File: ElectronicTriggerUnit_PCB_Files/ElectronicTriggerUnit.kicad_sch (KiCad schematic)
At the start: 50 parts, among them IC1 MCP1407-E_SN, IC2 ATTINY814-SSF, IC3 BU4S584G2-TR, J2 Conn_01x05, J4 Conn_01x04, M1 Motor_DC, Q1 LC191PTDT, Q2 LKPT30102B-A01, Q3 SIR500DP-T1-RE3, Q4 LC191PTDT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

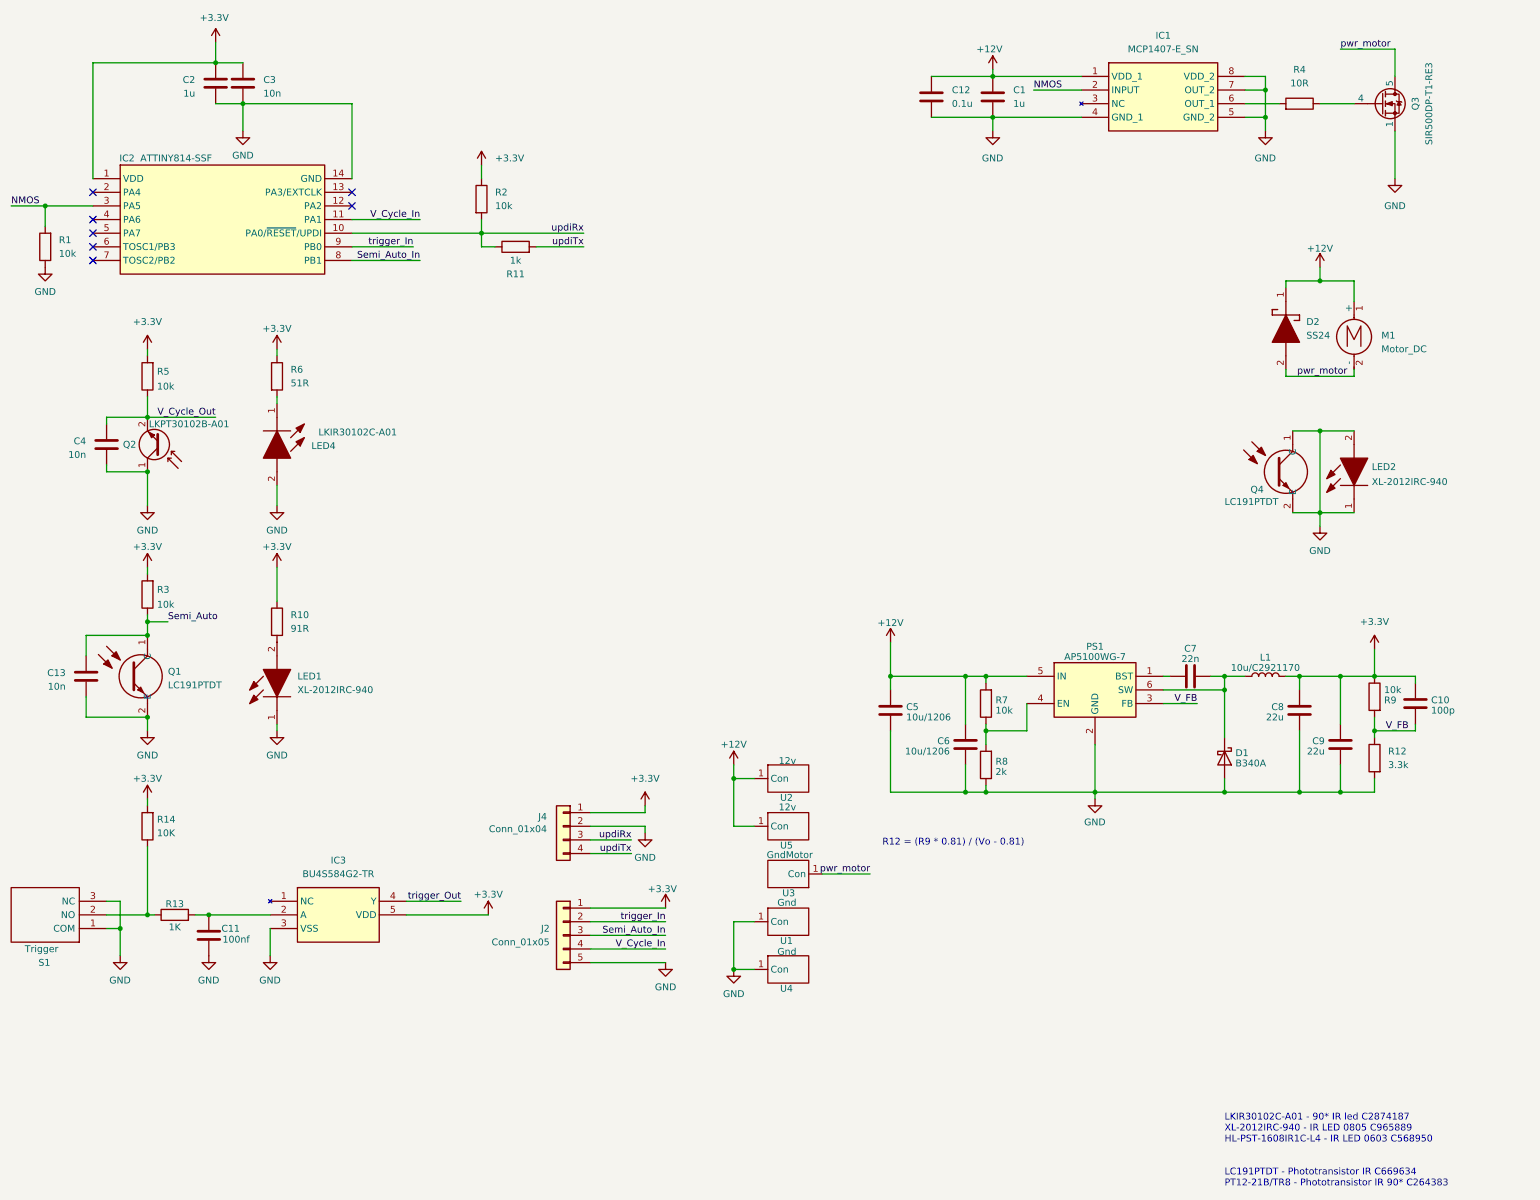
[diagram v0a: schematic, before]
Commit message: added motor ring
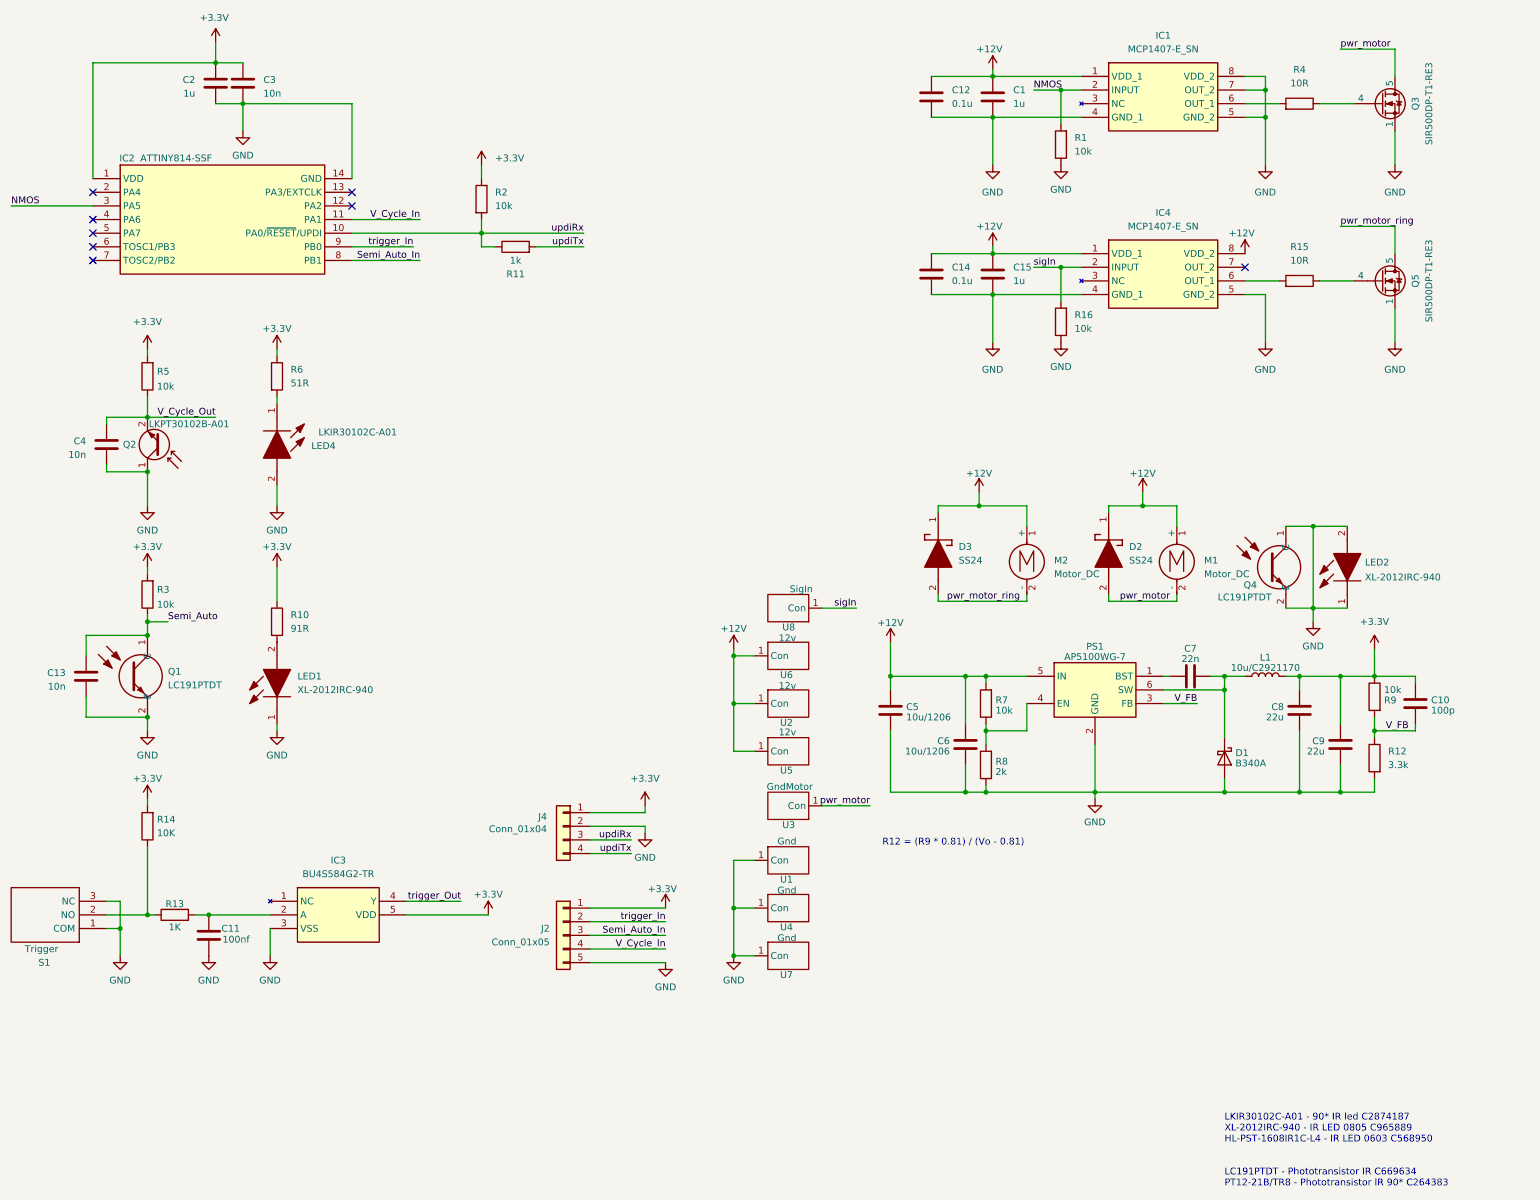
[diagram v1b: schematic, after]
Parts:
- added C14: 0.1u, Capacitor_SMD:C_0603_1608Metric, symbol Device:C
- added C15: 1u, Capacitor_SMD:C_0603_1608Metric, symbol Device:C
- added D3: SS24, SamacSys:DIOM5436X247N, symbol SamacSys:SS24
- added IC4: MCP1407-E_SN, SamacSys:SOIC127P600X175-8N, symbol SamacSys:MCP1407-E_SN
- added M2: Motor_DC, symbol Motor:Motor_DC
- added Q5: SIR500DP-T1-RE3, SamacSys:POWERPAKSO-8, symbol Simulation_SPICE:NMOS
- added R15: 10R, Resistor_SMD:R_1206_3216Metric, symbol Device:R
- added R16: 10k, Resistor_SMD:R_0603_1608Metric, symbol Device:R
- added U6: 12v, SamacSys:Copper_Pad, symbol Copper_Pad:Copper_pad
- added U7: Gnd, SamacSys:Copper_Pad, symbol Copper_Pad:Copper_pad
- added U8: SigIn, SamacSys:Copper_Pad, symbol Copper_Pad:Copper_pad
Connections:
- net +12V: now also C14.1, C15.2, D3.1 (K), IC4.1 (VDD_1), IC4.8 (VDD_2), M2.1 (+), U6.1 (Con)
- net GND: now also C14.2, C15.1, IC4.4 (GND_1), IC4.5 (GND_2), Q5.1, Q5.2, Q5.3, R16.1, U7.1 (Con)
- new net: IC4.6 (OUT_1), R15.2
- new net: Q5.4, R15.1
- new net pwr_motor_ring: D3.2 (A), M2.2 (-), Q5.5, Q5.6, Q5.7, Q5.8, Q5.9
- new net sigIn: IC4.2 (INPUT), R16.2, U8.1 (Con)
- no-connect marks 7 -> 8
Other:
- moved on the sheet: D2, LED2, M1, Q4, R1, U1, U2, U3, U4, U5

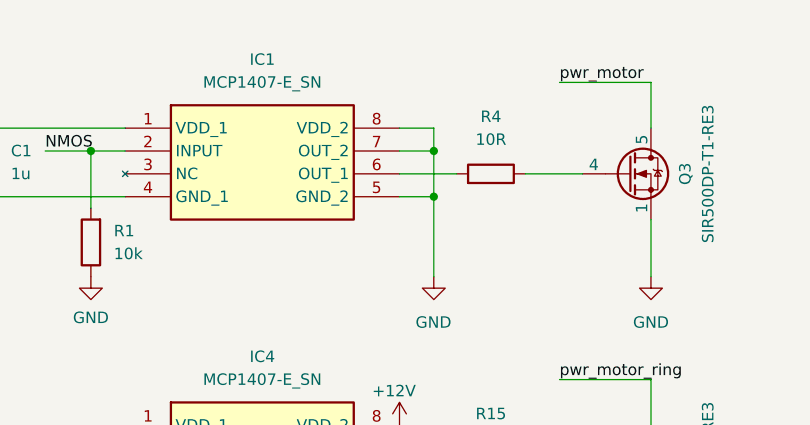
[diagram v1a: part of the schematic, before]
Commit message: outputs of gate driver needed to be shorted :(
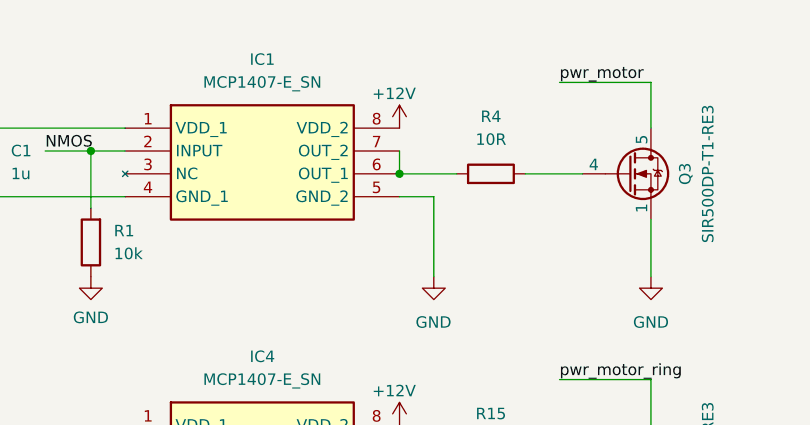
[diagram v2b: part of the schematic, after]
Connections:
- net +12V: now also IC1.8 (VDD_2)
- net GND: no longer IC1.7 (OUT_2), IC1.8 (VDD_2)
- net at IC1.6 (OUT_1), R4.2: now also IC1.7 (OUT_2)
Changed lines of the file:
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@@
 	)
 	(junction
-		(at 248.92 27.94)
-		(diameter 0)
-		(color 0 0 0 0)
-	)
-	(junction
 		(at 226.06 105.41)
 		(diameter 0)
@@
 	)
 	(junction
+		(at 245.11 30.48)
+		(diameter 0)
+		(color 0 0 0 0)
+	)
+	(junction
 		(at 198.12 66.04)
 		(diameter 0)
@@
 	)
 	(junction
-		(at 248.92 33.02)
-		(diameter 0)
-		(color 0 0 0 0)
-	)
-	(junction
 		(at 196.85 137.16)
 		(diameter 0)
@@
 	(wire
 		(pts
-			(xy 248.92 27.94) (xy 248.92 33.02)
-		)
-		(stroke
-			(width 0)
-			(type default)
-		)
-	)
-	(wire
-		(pts
 			(xy 149.86 133.35) (xy 149.86 142.24)
 		)
@@
 	(wire
 		(pts
-			(xy 245.11 27.94) (xy 248.92 27.94)
-		)
-		(stroke
-			(width 0)
-			(type default)
-		)
-	)
-	(wire
-		(pts
 			(xy 269.24 132.08) (xy 269.24 137.16)
 		)
@@
 	(wire
 		(pts
-			(xy 245.11 25.4) (xy 248.92 25.4)
-		)
-		(stroke
-			(width 0)
-			(type default)
-		)
-	)
-	(wire
-		(pts
 			(xy 186.69 58.42) (xy 198.12 58.42)
 		)
@@
 	(wire
 		(pts
+			(xy 245.11 27.94) (xy 245.11 30.48)
+		)
+		(stroke
+			(width 0)
+			(type default)
+		)
+	)
+	(wire
+		(pts
 			(xy 276.86 137.16) (xy 276.86 138.43)
 		)
@@
 	(wire
 		(pts
-			(xy 248.92 25.4) (xy 248.92 27.94)
-		)
-		(stroke
-			(width 0)
-			(type default)
-		)
-	)
-	(wire
-		(pts
 			(xy 40.64 76.2) (xy 40.64 77.47)
 		)
@@
 					(unit 1)
 				)
+			)
+		)
+	)
+	(symbol
+		(lib_name "+12V_1")
+		(lib_id "power:+12V")
+		(at 245.11 25.4 0)
+		(unit 1)
+		(exclude_from_sim no)
+		(in_bom yes)
+		(on_board yes)
+		(dnp no)
+		(property "Reference" "#PWR040"
+			(at 245.11 29.21 0)
+			(effects
+				(font
+					(size 1.27 1.27)
+				)
+				(hide yes)
+			)
+		)
+		(property "Value" "+12V"
+			(at 242.062 21.59 0)
+			(effects
+				(font
+					(size 1.27 1.27)
+				)
+				(justify left)
+			)
+		)
+		(property "Footprint" ""
+			(at 245.11 25.4 0)
+			(effects
+				(font
+					(size 1.27 1.27)
+				)
+				(hide yes)
+			)
+		)
+		(property "Datasheet" ""
+			(at 245.11 25.4 0)
+			(effects
+				(font
+					(size 1.27 1.27)
+				)
+				(hide yes)
+			)
+		)
+		(property "Description" "Power symbol creates a global label with name \"+12V\""
+			(at 245.11 25.4 0)
+			(effects
+				(font
+					(size 1.27 1.27)
+				)
+				(hide yes)
+			)
+		)
+		(pin "1"
+		)
+		(instances
+			(project "ElectronicTriggerUnit"
+				(path "/006bc43b-d3a8-4a38-a8dc-5a24da3f9b4d"
+					(reference "#PWR040")
+					(unit 1)
+				)
